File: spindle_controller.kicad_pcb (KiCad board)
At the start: 2 copper layers, 62 x 124.5 mm, 70 parts, among them J1 VAC 230V, J2 AUX/CONTROL, J3 ICP, J4 Load output, J5 CONN_01X03, J6 CONN_01X03, J7 GND_JUMPER, J8 VCC_JUMPER, J9 Jack_3.5mm_4pin, Q1 2N3904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

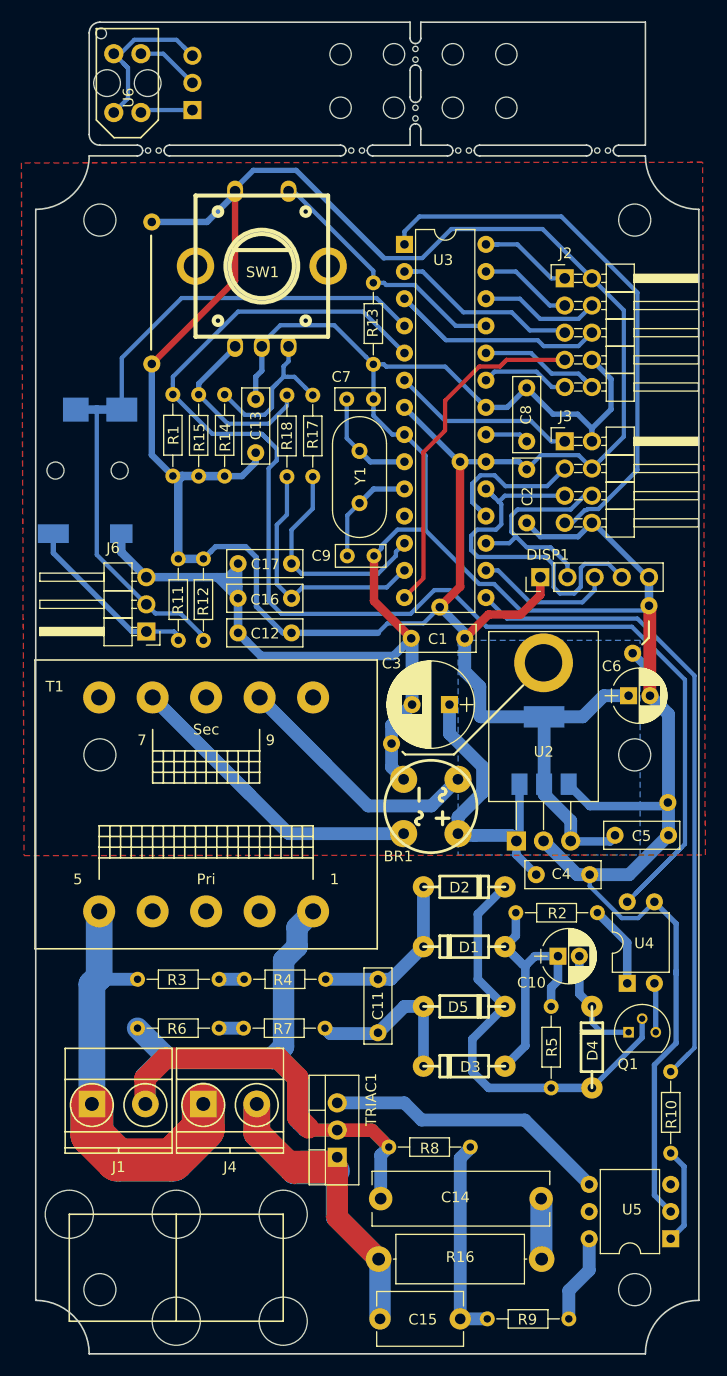
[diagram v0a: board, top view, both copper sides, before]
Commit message: Add reset button
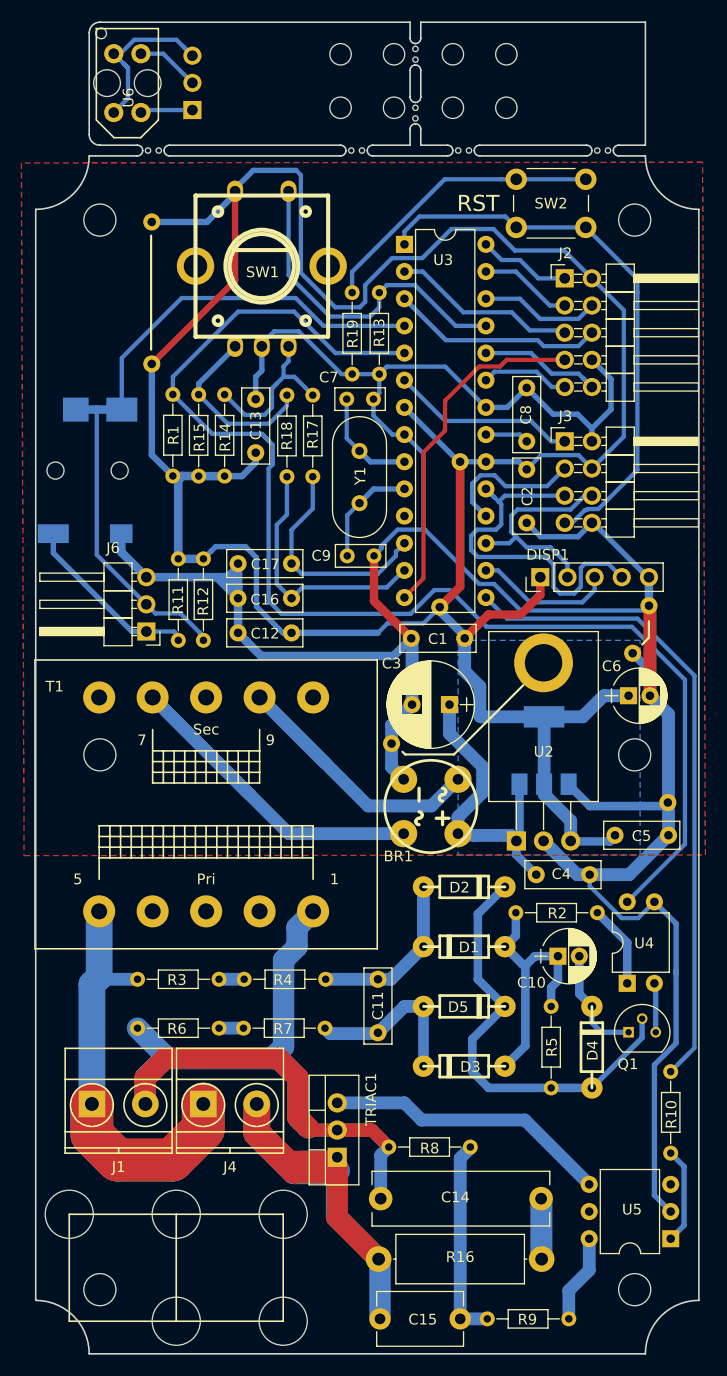
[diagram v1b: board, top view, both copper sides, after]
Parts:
- added R19: 360, Resistors_ThroughHole:R_Axial_DIN0204_L3.6mm_D1.6mm_P7.62mm_Horizontal, F.Cu at (88.9, 61.7)
- added SW2: SW_SPST, Buttons_Switches_ThroughHole:SW_PUSH_6mm, F.Cu at (110.7, 55.6)
- moved R13 1.07 mm to (91.4, 69.3)
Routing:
- net Net-(R19-Pad1): track 0.00 -> 27.4 mm
- net VCC: track 240.2 -> 250.3 mm
- net /SW1: track 24.3 -> 32.0 mm
- net /ZCROSS_PULSE: track 127.5 -> 121.2 mm
- net GND: track 284.2 -> 282.4 mm
- net /SCL: track 9.81 -> 8.68 mm
- net /RST: track 51.9 -> 52.7 mm
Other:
- board text added: "RST"
